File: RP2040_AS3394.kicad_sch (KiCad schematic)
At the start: 33 parts

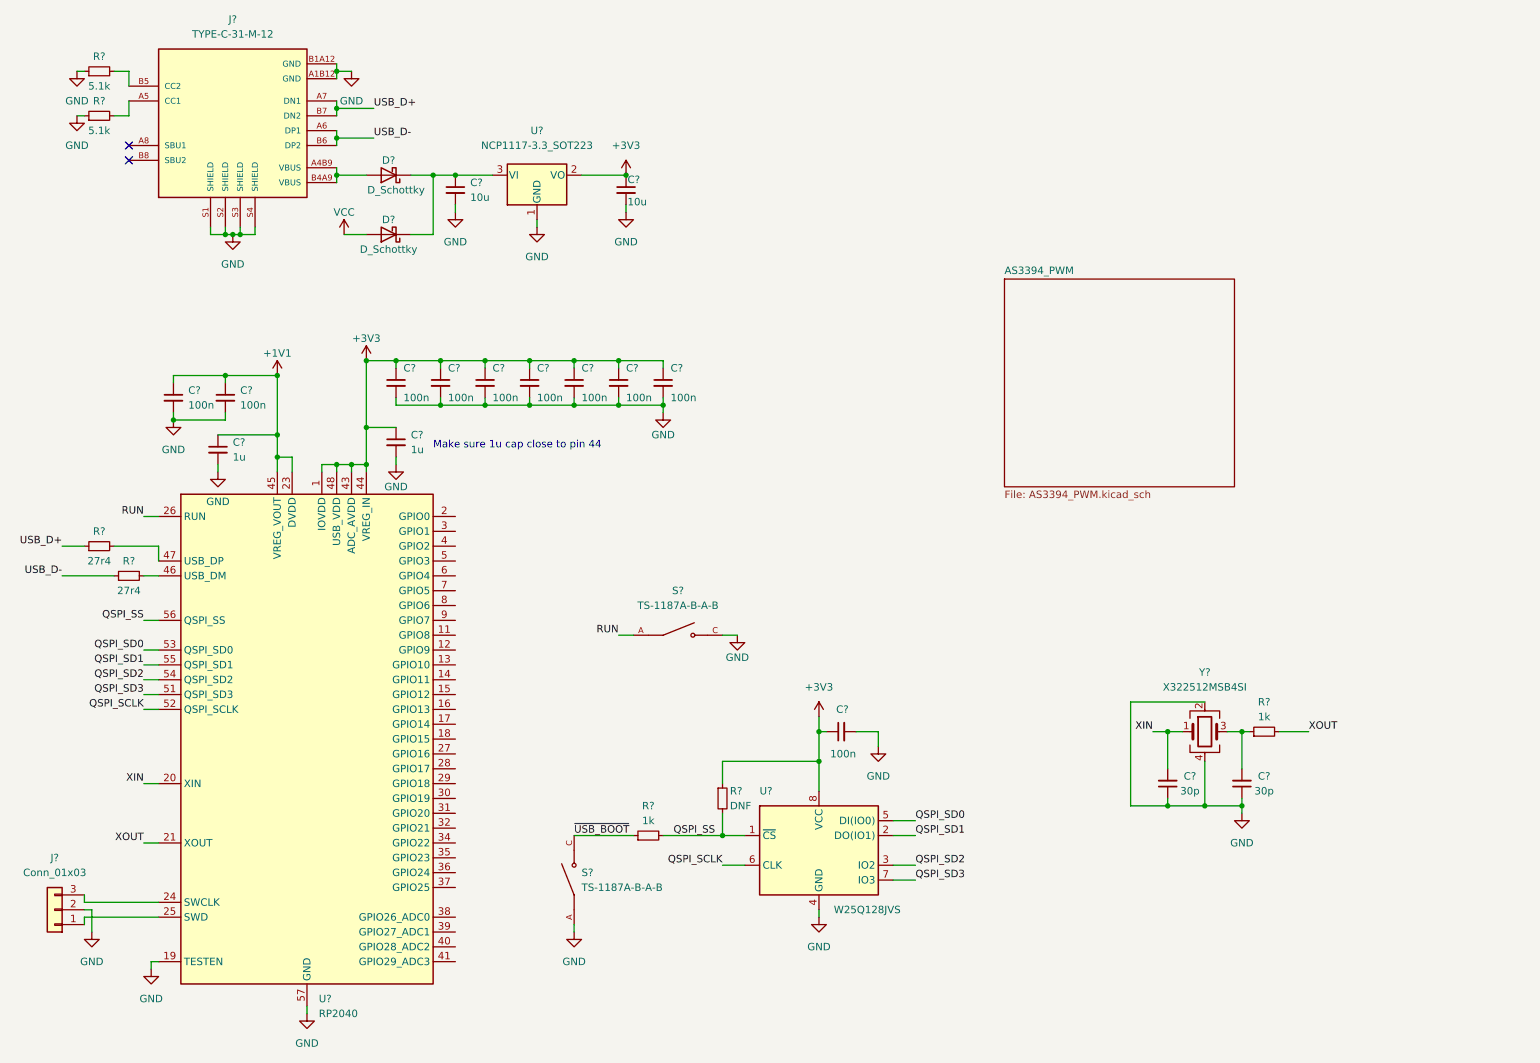
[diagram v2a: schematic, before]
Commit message: Added PWM connections from RP2040 to subsheet containing AS3394; finished assinging components for JLC assembly
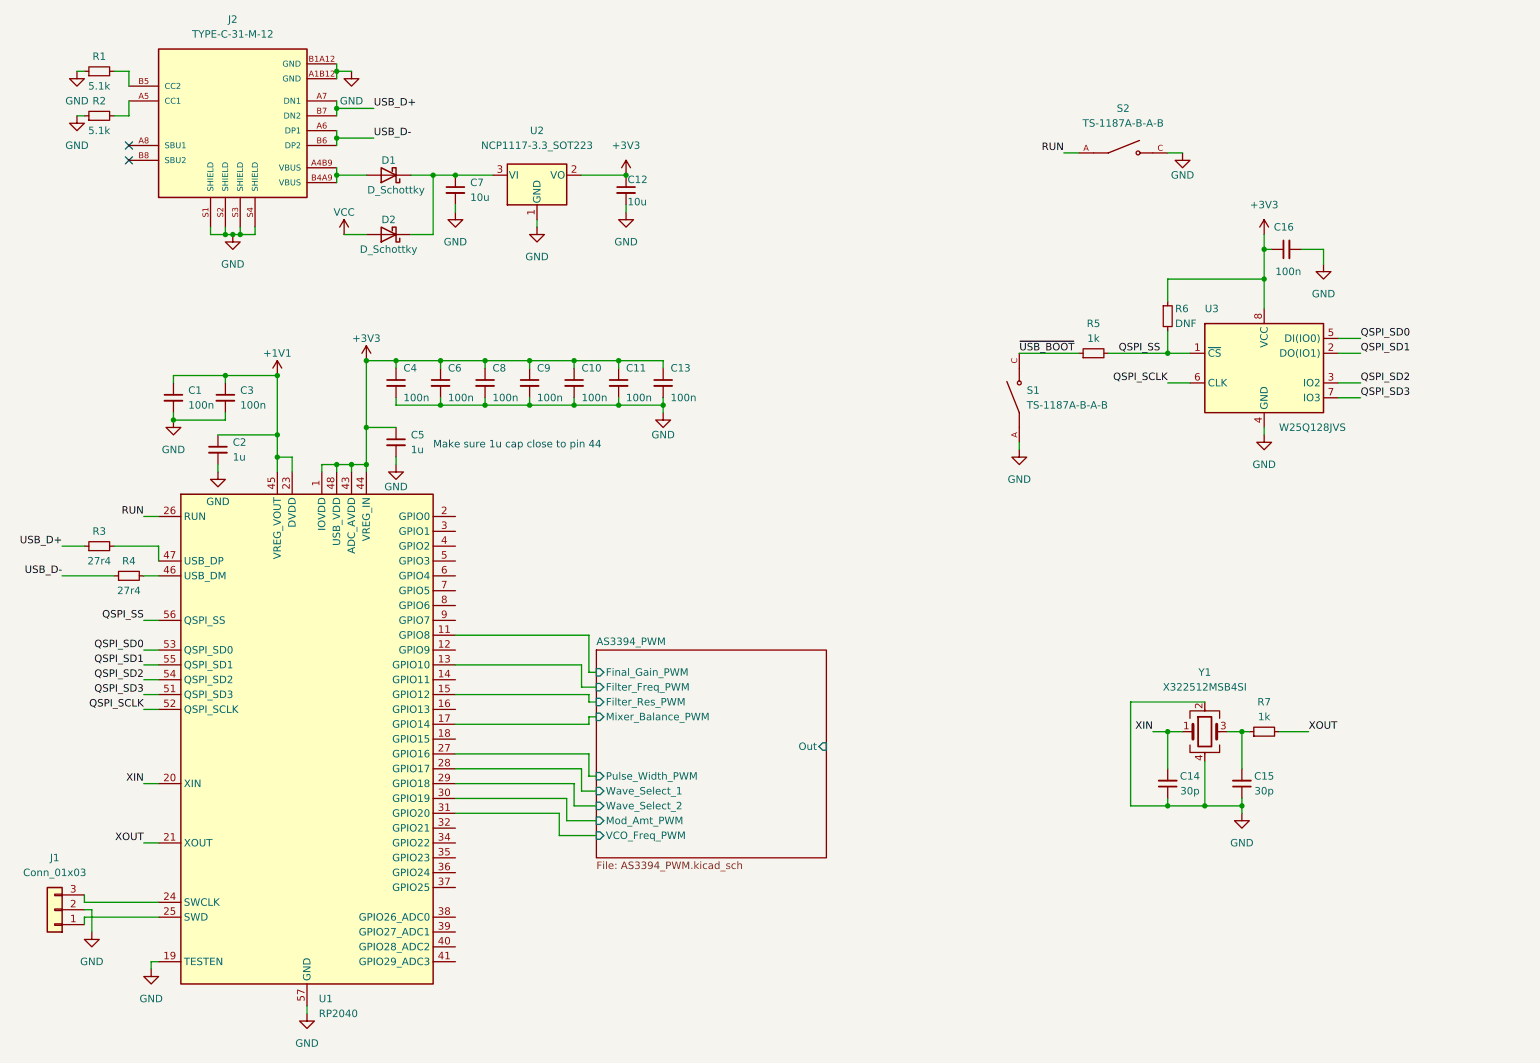
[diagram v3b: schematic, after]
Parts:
- C1, C10, C11, C13, C2, C3, C4, C5, C6, C8, C9: renamed from C?; footprint (none) -> Capacitor_SMD:C_0402_1005Metric
- C12, C16, C7: renamed from C?; footprint (none) -> Capacitor_SMD:C_0603_1608Metric
- C14, C15: renamed from C?; footprint (none) -> Capacitor_SMD:C_01005_0402Metric
- D1, D2: renamed from D?; footprint (none) -> Diode_SMD:D_SMA
- J1: renamed from J?; footprint (none) -> Connector_PinHeader_2.54mm:PinHeader_1x03_P2.54mm_Vertical
- R1, R2, R5, R6, R7: renamed from R?; footprint (none) -> Resistor_SMD:R_0402_1005Metric
- R3, R4: renamed from R?; footprint (none) -> Resistor_SMD:R_0603_1608Metric
- S1, S2: renamed from S?; footprint SW_TS-1187A-B-A-B -> footprints:SW_TS-1187A-B-A-B
- Y1: renamed from Y?; footprint (none) -> Crystal:Crystal_SMD_3225-4Pin_3.2x2.5mm
- gave numbers to parts that had none: 4
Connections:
- net AS3394_PWM/Final_Gain_PWM: now reaches U1.11 (GPIO8)
- net AS3394_PWM/Filter_Freq_PWM: now reaches U1.13 (GPIO10)
- net AS3394_PWM/Filter_Res_PWM: now reaches U1.15 (GPIO12)
- net AS3394_PWM/Mixer_Balance_PWM: now reaches U1.17 (GPIO14)
- net AS3394_PWM/Pulse_Width_PWM: now reaches U1.27 (GPIO16)
- net AS3394_PWM/Wave_Select_1: now reaches U1.28 (GPIO17)
- net AS3394_PWM/Wave_Select_2: now reaches U1.29 (GPIO18)
- net AS3394_PWM/Mod_Amt_PWM: now reaches U1.30 (GPIO19)
- net AS3394_PWM/VCO_Freq_PWM: now reaches U1.31 (GPIO20)
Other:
- sheet AS3394_PWM ports: added Filter_Freq_PWM, Filter_Res_PWM, Final_Gain_PWM, Mixer_Balance_PWM, Mod_Amt_PWM, Out, Pulse_Width_PWM, VCO_Freq_PWM, Wave_Select_1, Wave_Select_2; removed none
- moved on the sheet: C16, R5, R6, S1, S2, U3

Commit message: Started placement
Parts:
- R3, R4: footprint Resistor_SMD:R_0603_1608Metric -> Resistor_SMD:R_0402_1005Metric
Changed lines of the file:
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@@
     (property "Reference" "R4" (id 0) (at 36.83 110.49 90))
     (property "Value" "27r4" (id 1) (at 36.83 115.57 90))
-    (property "Footprint" "Resistor_SMD:R_0603_1608Metric" (id 2) (at 36.83 113.03 0)
+    (property "Footprint" "Resistor_SMD:R_0402_1005Metric" (id 2) (at 36.83 113.03 0)
       (effects (font (size 1.27 1.27)) hide)
     )
@@
     (property "Reference" "R3" (id 0) (at 31.75 105.41 90))
     (property "Value" "27r4" (id 1) (at 31.75 110.49 90))
-    (property "Footprint" "Resistor_SMD:R_0603_1608Metric" (id 2) (at 31.75 107.95 0)
+    (property "Footprint" "Resistor_SMD:R_0402_1005Metric" (id 2) (at 31.75 107.95 0)
       (effects (font (size 1.27 1.27)) hide)
     )
@@
     )
     (path "/fb7a6a2b-6d32-4492-b5c5-aaea7b40b6e9"
-      (reference "R3") (unit 1) (value "27r4") (footprint "Resistor_SMD:R_0603_1608Metric")
+      (reference "R3") (unit 1) (value "27r4") (footprint "Resistor_SMD:R_0402_1005Metric")
     )
     (path "/24df9397-4e6f-4253-87dd-9783e343297e"
-      (reference "R4") (unit 1) (value "27r4") (footprint "Resistor_SMD:R_0603_1608Metric")
+      (reference "R4") (unit 1) (value "27r4") (footprint "Resistor_SMD:R_0402_1005Metric")
     )
     (path "/c9125209-3096-4fe8-91c7-84881ea1f68d"
@@
       (reference "U4") (unit 3) (value "LM324") (footprint "Package_SO:SOIC-14_3.9x8.7mm_P1.27mm")
     )
-    (path "/4be0f50f-df7d-4a82-b90c-e414038b561e/229825aa-f5ba-4ffd-af61-f3666b3b954e"
+    (path "/4be0f50f-df7d-4a82-b90c-e414038b561e/d6eb3b1b-16c0-4565-9e04-4b99751ec30b"
       (reference "U4") (unit 4) (value "LM324") (footprint "Package_SO:SOIC-14_3.9x8.7mm_P1.27mm")
     )
@@
       (reference "U5") (unit 1) (value "AS3394") (footprint "Package_DIP:DIP-24_W7.62mm_Socket")
     )
-    (path "/4be0f50f-df7d-4a82-b90c-e414038b561e/d6eb3b1b-16c0-4565-9e04-4b99751ec30b"
+    (path "/4be0f50f-df7d-4a82-b90c-e414038b561e/229825aa-f5ba-4ffd-af61-f3666b3b954e"
       (reference "U6") (unit 1) (value "LM324") (footprint "Package_SO:SOIC-14_3.9x8.7mm_P1.27mm")
     )

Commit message: Finished most of routing; added TL071 for headphone out; working on adding I/O
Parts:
- added C50, C51: 0.1u, Capacitor_SMD:C_0402_1005Metric, symbol Device:C_Small
- added C52: 47p, Capacitor_SMD:C_0402_1005Metric, symbol Device:C_Small
- added J3: Conn_01x02, Connector_PinHeader_2.54mm:PinHeader_1x02_P2.54mm_Vertical, symbol Connector_Generic:Conn_01x02
- added J5: Conn_01x03, Connector_PinHeader_2.54mm:PinHeader_1x03_P2.54mm_Vertical, symbol Connector_Generic:Conn_01x03
- added R16: 7.5k, Resistor_SMD:R_0402_1005Metric, symbol Device:R_Small
- added U7: TL071, Package_SO:SOIC-8_3.9x4.9mm_P1.27mm, symbol Amplifier_Operational:TL071
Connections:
- net AS3394_PWM/Filter_Freq_PWM: now also U1.11 (GPIO8); no longer U1.13 (GPIO10)
- net AS3394_PWM/Filter_Res_PWM: now also U1.13 (GPIO10); no longer U1.15 (GPIO12)
- net AS3394_PWM/Final_Gain_PWM: now also U1.15 (GPIO12); no longer U1.11 (GPIO8)
- net AS3394_PWM/Out: now also U7.2 (-)
- net GND: now also C50.2, C51.2, J3.2 (Pin_2), J5.2 (Pin_2); no longer J2.S1 (SHIELD), J2.S2 (SHIELD), J2.S3 (SHIELD), J2.S4 (SHIELD)
- net VCC: now also C50.1, J5.1 (Pin_1), U7.7 (V+)
- net AMP_OUT: now reaches U1.38 (GPIO26_ADC0)
- net AMP_OUT: now also C52.2, J3.1 (Pin_1), R16.2, U7.6
- new net: C52.1, R16.1, U7.3 (+)
- new net VEE: C51.1, J5.3 (Pin_3), U7.4 (V-)
- no-connect marks 2 -> 8
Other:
- moved on the sheet: C14, C15, R7, Y1

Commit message: Mostly finished, just need to review and add final touches
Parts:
- added J4: Conn_01x08, Connector_PinHeader_2.54mm:PinHeader_1x08_P2.54mm_Vertical, symbol Connector_Generic:Conn_01x08
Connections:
- net AS3394_PWM/Wave_Select_1: now also U1.29 (GPIO18); no longer U1.28 (GPIO17)
- net AS3394_PWM/Wave_Select_2: now also U1.28 (GPIO17); no longer U1.29 (GPIO18)
- net at U1.2 (GPIO0): now also J4.1 (Pin_1)
- net at U1.3 (GPIO1): now also J4.2 (Pin_2)
- net at U1.4 (GPIO2): now also J4.3 (Pin_3)
- net at U1.5 (GPIO3): now also J4.4 (Pin_4)
- net at U1.6 (GPIO4): now also J4.5 (Pin_5)
- net at U1.7 (GPIO5): now also J4.6 (Pin_6)
- net at U1.8 (GPIO6): now also J4.7 (Pin_7)
- net at U1.9 (GPIO7): now also J4.8 (Pin_8)
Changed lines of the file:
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@@
+    (stroke (width 0) (type default) (color 0 0 0 0))
+  )
+  (wire (pts (xy 92.71 102.87) (xy 96.52 102.87))
     (stroke (width 0) (type default) (color 0 0 0 0))
   )
@@
     (stroke (width 0) (type default) (color 0 0 0 0))
   )
+  (wire (pts (xy 92.71 107.95) (xy 96.52 107.95))
+    (stroke (width 0) (type default) (color 0 0 0 0))
+  )
   (wire (pts (xy 246.38 153.67) (xy 246.38 154.94))
     (stroke (width 0) (type default) (color 0 0 0 0))
@@
     (stroke (width 0) (type default) (color 0 0 0 0))
   )
+  (wire (pts (xy 92.71 120.65) (xy 96.52 120.65))
+    (stroke (width 0) (type default) (color 0 0 0 0))
+  )
   (wire (pts (xy 175.26 129.54) (xy 176.53 129.54))
     (stroke (width 0) (type default) (color 0 0 0 0))
@@
     (stroke (width 0) (type default) (color 0 0 0 0))
   )
+  (wire (pts (xy 92.71 115.57) (xy 96.52 115.57))
+    (stroke (width 0) (type default) (color 0 0 0 0))
+  )
   (wire (pts (xy 105.41 76.2) (xy 113.03 76.2))
     (stroke (width 0) (type default) (color 0 0 0 0))
@@
     (stroke (width 0) (type default) (color 0 0 0 0))
   )
+  (wire (pts (xy 92.71 118.11) (xy 96.52 118.11))
+    (stroke (width 0) (type default) (color 0 0 0 0))
+  )
   (wire (pts (xy 90.17 83.82) (xy 97.79 83.82))
     (stroke (width 0) (type default) (color 0 0 0 0))
@@
     (stroke (width 0) (type default) (color 0 0 0 0))
   )
+  (wire (pts (xy 92.71 110.49) (xy 96.52 110.49))
+    (stroke (width 0) (type default) (color 0 0 0 0))
+  )
   (wire (pts (xy 72.39 93.98) (xy 74.93 93.98))
     (stroke (width 0) (type default) (color 0 0 0 0))
@@
     (stroke (width 0) (type default) (color 0 0 0 0))
   )
+  (wire (pts (xy 92.71 105.41) (xy 96.52 105.41))
+    (stroke (width 0) (type default) (color 0 0 0 0))
+  )
+  (wire (pts (xy 113.03 152.4) (xy 116.84 152.4))
+    (stroke (width 0) (type default) (color 0 0 0 0))
+  )
   (wire (pts (xy 259.08 153.67) (xy 259.08 154.94))
     (stroke (width 0) (type default) (color 0 0 0 0))
@@
     (stroke (width 0) (type default) (color 0 0 0 0))
   )
+  (wire (pts (xy 114.3 149.86) (xy 116.84 149.86))
+    (stroke (width 0) (type default) (color 0 0 0 0))
+  )
   (wire (pts (xy 39.37 133.35) (xy 41.91 133.35))
     (stroke (width 0) (type default) (color 0 0 0 0))
@@
     (stroke (width 0) (type default) (color 0 0 0 0))
   )
-  (wire (pts (xy 113.03 152.4) (xy 116.84 152.4))
-    (stroke (width 0) (type default) (color 0 0 0 0))
-  )
   (wire (pts (xy 39.37 125.73) (xy 41.91 125.73))
     (stroke (width 0) (type default) (color 0 0 0 0))
   )
+  (wire (pts (xy 92.71 113.03) (xy 96.52 113.03))
+    (stroke (width 0) (type default) (color 0 0 0 0))
+  )
   (wire (pts (xy 191.77 114.3) (xy 190.5 114.3))
     (stroke (width 0) (type default) (color 0 0 0 0))
@@
   )
   (wire (pts (xy 105.41 82.55) (xy 105.41 83.82))
-    (stroke (width 0) (type default) (color 0 0 0 0))
-  )
-  (wire (pts (xy 114.3 149.86) (xy 116.84 149.86))
     (stroke (width 0) (type default) (color 0 0 0 0))
   )
@@
     (pin "1")
     (pin "2")
+  )
+  (symbol (lib_id "Connector_Generic:Conn_01x08") (at 101.6 110.49 0) (unit 1)
+    (in_bom yes) (on_board yes) (fields_autoplaced)
+    (property "Reference" "J4" (id 0) (at 104.14 110.4899 0)
+      (effects (font (size 1.27 1.27)) (justify left))
+    )
+    (property "Value" "Conn_01x08" (id 1) (at 104.14 113.0299 0)
+      (effects (font (size 1.27 1.27)) (justify left))
+    )
+    (property "Footprint" "Connector_PinHeader_2.54mm:PinHeader_1x08_P2.54mm_Vertical" (id 2) (at 101.6 110.49 0)
+      (effects (font (size 1.27 1.27)) hide)
+    )
+    (property "Datasheet" "~" (id 3) (at 101.6 110.49 0)
+      (effects (font (size 1.27 1.27)) hide)
+    )
+    (pin "1")
+    (pin "2")
+    (pin "3")
+    (pin "4")
+    (pin "5")
+    (pin "6")
+    (pin "7")
+    (pin "8")
   )
   (symbol (lib_id "power:GND") (at 92.71 50.8 0) (unit 1)
@@
       (effects (font (size 1.27 1.27)) (justify left))
     )
-    (pin "Wave_Select_2" input (at 116.84 152.4 180)
-      (effects (font (size 1.27 1.27)) (justify left))
-    )
-    (pin "Wave_Select_1" input (at 116.84 149.86 180)
+    (pin "Wave_Select_2" input (at 116.84 149.86 180)
+      (effects (font (size 1.27 1.27)) (justify left))
+    )
+    (pin "Wave_Select_1" input (at 116.84 152.4 180)
       (effects (font (size 1.27 1.27)) (justify left))
     )
@@
       (reference "J3") (unit 1) (value "Conn_01x02") (footprint "Connector_PinHeader_2.54mm:PinHeader_1x02_P2.54mm_Vertical")
     )
+    (path "/2ce704f0-1cd2-4f01-8fb4-4a3ec593dfc3"
+      (reference "J4") (unit 1) (value "Conn_01x08") (footprint "Connector_PinHeader_2.54mm:PinHeader_1x08_P2.54mm_Vertical")
+    )
     (path "/564fdaf2-e2d0-481b-bd85-71ffb7c91a1d"

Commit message: First board prototype ordered from JLC with assembly
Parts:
- C14, C15: footprint Capacitor_SMD:C_01005_0402Metric -> Capacitor_SMD:C_0402_1005Metric
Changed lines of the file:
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@@
     (property "Reference" "C15" (id 0) (at 262.89 149.86 0))
     (property "Value" "30p" (id 1) (at 262.89 152.4 0))
-    (property "Footprint" "Capacitor_SMD:C_01005_0402Metric" (id 2) (at 259.08 151.13 0)
+    (property "Footprint" "Capacitor_SMD:C_0402_1005Metric" (id 2) (at 259.08 151.13 0)
       (effects (font (size 1.27 1.27)) hide)
     )
@@
     (property "Reference" "C14" (id 0) (at 250.19 149.86 0))
     (property "Value" "30p" (id 1) (at 250.19 152.4 0))
-    (property "Footprint" "Capacitor_SMD:C_01005_0402Metric" (id 2) (at 246.38 151.13 0)
+    (property "Footprint" "Capacitor_SMD:C_0402_1005Metric" (id 2) (at 246.38 151.13 0)
       (effects (font (size 1.27 1.27)) hide)
     )
@@
     )
     (path "/fb735d34-ce15-452b-aa4b-4c329fb152ca"
-      (reference "C14") (unit 1) (value "30p") (footprint "Capacitor_SMD:C_01005_0402Metric")
+      (reference "C14") (unit 1) (value "30p") (footprint "Capacitor_SMD:C_0402_1005Metric")
     )
     (path "/2c93ca02-d736-4597-af42-e489fc6b236f"
-      (reference "C15") (unit 1) (value "30p") (footprint "Capacitor_SMD:C_01005_0402Metric")
+      (reference "C15") (unit 1) (value "30p") (footprint "Capacitor_SMD:C_0402_1005Metric")
     )
     (path "/e61cd687-5e03-4b49-adac-2cf6ff1b207a"
@@
     )
     (path "/4be0f50f-df7d-4a82-b90c-e414038b561e/66fc3cfc-f53a-4e36-89f2-50180c9648db"
-      (reference "C20") (unit 1) (value "10n") (footprint "Capacitor_SMD:C_01005_0402Metric")
+      (reference "C20") (unit 1) (value "10n") (footprint "Capacitor_SMD:C_0402_1005Metric")
     )
     (path "/4be0f50f-df7d-4a82-b90c-e414038b561e/037f6d27-3bd9-456e-a486-1a993d911919"
@@
     )
     (path "/4be0f50f-df7d-4a82-b90c-e414038b561e/414b309d-30ee-48b5-974c-f813a593629b"
-      (reference "R20") (unit 1) (value "3k") (footprint "Resistor_SMD:R_0201_0603Metric")
+      (reference "R20") (unit 1) (value "3k") (footprint "Resistor_SMD:R_0603_1608Metric")
     )
     (path "/4be0f50f-df7d-4a82-b90c-e414038b561e/b02ef5d9-c3d1-41d1-bd80-f9a0bc559348"
@@
     )
     (path "/4be0f50f-df7d-4a82-b90c-e414038b561e/160be29f-8683-4bd3-bd62-a6f1b9b1d986"
-      (reference "R44") (unit 1) (value "33k") (footprint "Resistor_SMD:R_01005_0402Metric")
+      (reference "R44") (unit 1) (value "33k") (footprint "Resistor_SMD:R_0402_1005Metric")
     )
     (path "/4be0f50f-df7d-4a82-b90c-e414038b561e/4b5c3b3a-778b-4374-9e24-e58ceb263a60"

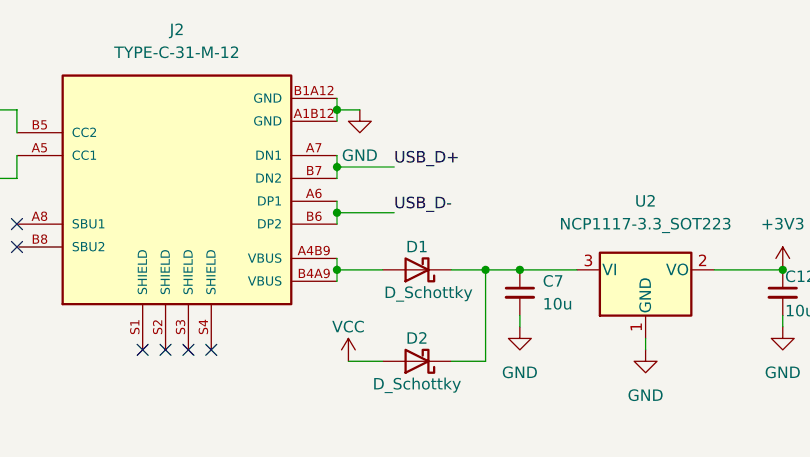
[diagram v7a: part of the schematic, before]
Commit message: Fixed diff pair polarity
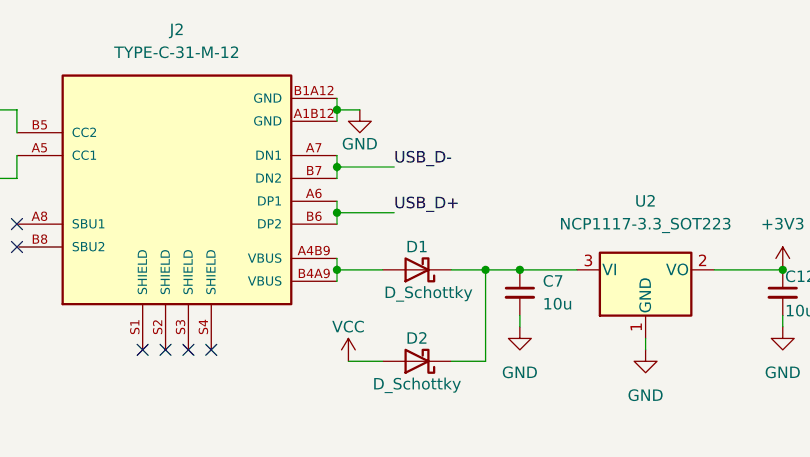
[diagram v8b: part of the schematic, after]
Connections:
- net USB_D+: now also J2.A6 (DP1), J2.B6 (DP2); no longer J2.A7 (DN1), J2.B7 (DN2)
- net USB_D-: now also J2.A7 (DN1), J2.B7 (DN2); no longer J2.A6 (DP1), J2.B6 (DP2)
